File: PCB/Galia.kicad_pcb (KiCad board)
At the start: 2 copper layers, 55 x 13.5 mm, 9 parts, among them J1 USB In, J2 USB, SW1 Bootsel, SW2 Reset, U2 TPD4E05U06

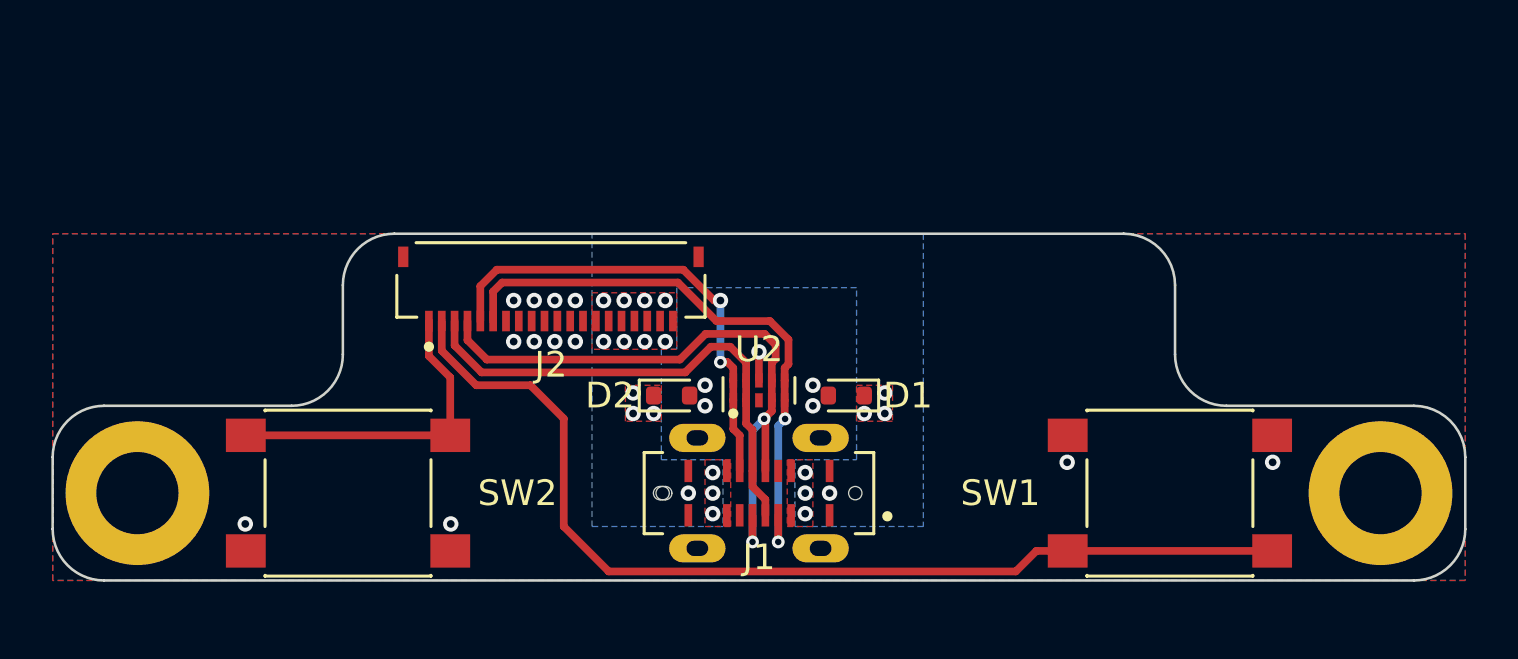
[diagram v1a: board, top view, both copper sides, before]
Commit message: 17/07/2023 update
Changed 20 pin FFC connector to 14 pin JST SH connector. Repositioned components.
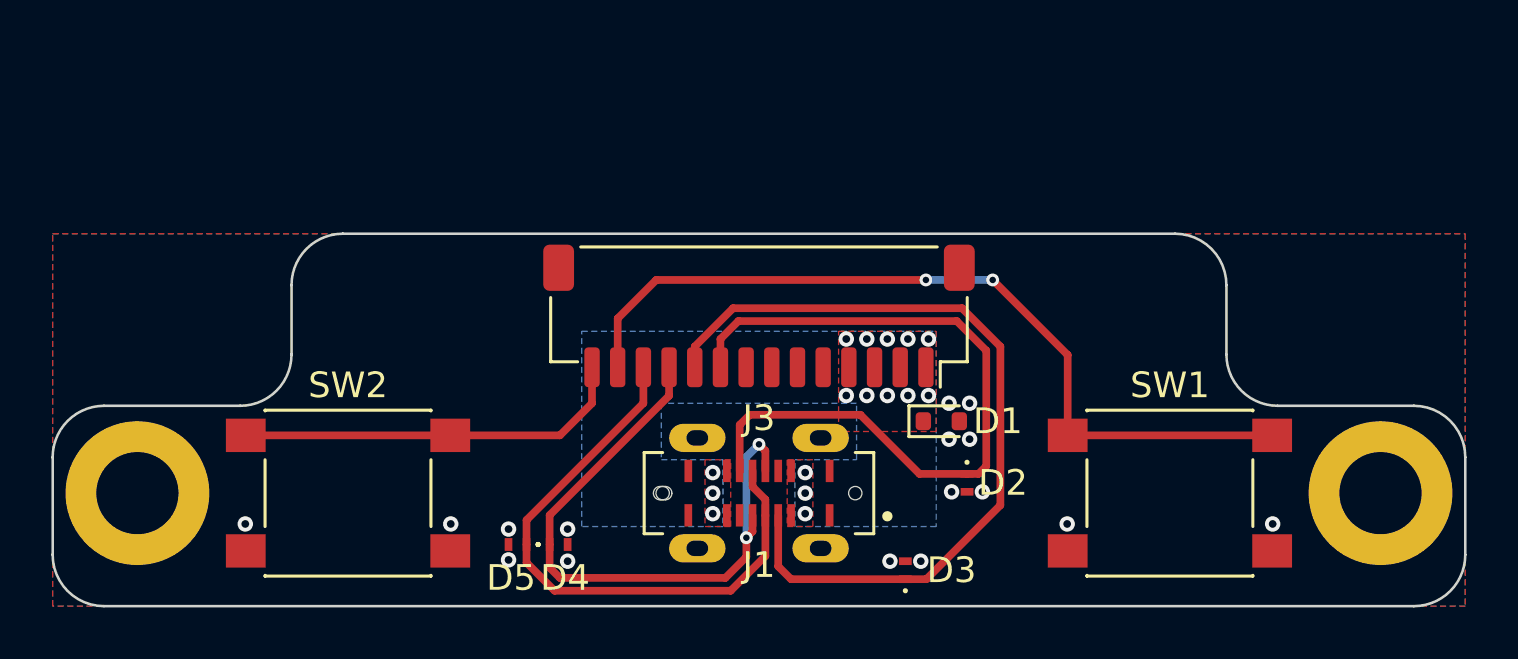
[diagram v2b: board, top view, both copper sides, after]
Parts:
- removed J2: USB, Galia:HRS_FH34SRJ-20S-0.5SH(50)
- removed U2: TPD4E05U06, Galia:USON-10_2.5x1.0mm_P0.5mm
- added D3: 5V, Galia:Texas_DPY0002A_0.6x1mm_P0.65mm, F.Cu at (95.7, 56.0)
- added D4: 5V, Galia:Texas_DPY0002A_0.6x1mm_P0.65mm, F.Cu at (82.2, 55.0)
- added D5: 5V, Galia:Texas_DPY0002A_0.6x1mm_P0.65mm, F.Cu at (80.6, 55.0)
- added J3: USB, Galia:JST_SH_SM14B-SRSS-TB_1x14-1MP_P1.00mm_Horizontal, F.Cu at (90.0, 46.1)
- D2: footprint Diode_SMD:D_SOD-523 -> Galia:Texas_DPY0002A_0.6x1mm_P0.65mm
- SW1: value Bootsel -> PTS45
- SW2: value Reset -> PTS45
- moved D2 12.0 mm to (98.1, 52.6), turned to -90 degrees
- moved D1 3.83 mm to (97.1, 50.2), turned to 0 degrees
- turned SW1 to 180 degrees
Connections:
- D2 pad 1: VBUS -> CC2
- SW1 pad 2: /BOOTSEL -> /~{RST}
- SW2 pad 2: /~{RST} -> /BOOTSEL
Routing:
- net /BOOTSEL: track 39.8 -> 15.4 mm
- net /~{RST}: track 12.8 -> 32.3 mm, vias 0 -> 2
- net CC2: track 18.6 -> 29.3 mm, vias 2 -> 0
- net CC1: track 22.8 -> 32.2 mm, vias 2 -> 0
- net /D+: track 19.7 -> 23.3 mm
- net GND: track 1.12 -> 0.00 mm, vias 19 -> 16
- net VBUS: vias 20 -> 16
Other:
- board size 55 x 13.5 mm -> 55 x 14.5 mm

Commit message: 18/07/2023 update.
Changed JST connector back to 20 pin FFC. Centered connector.
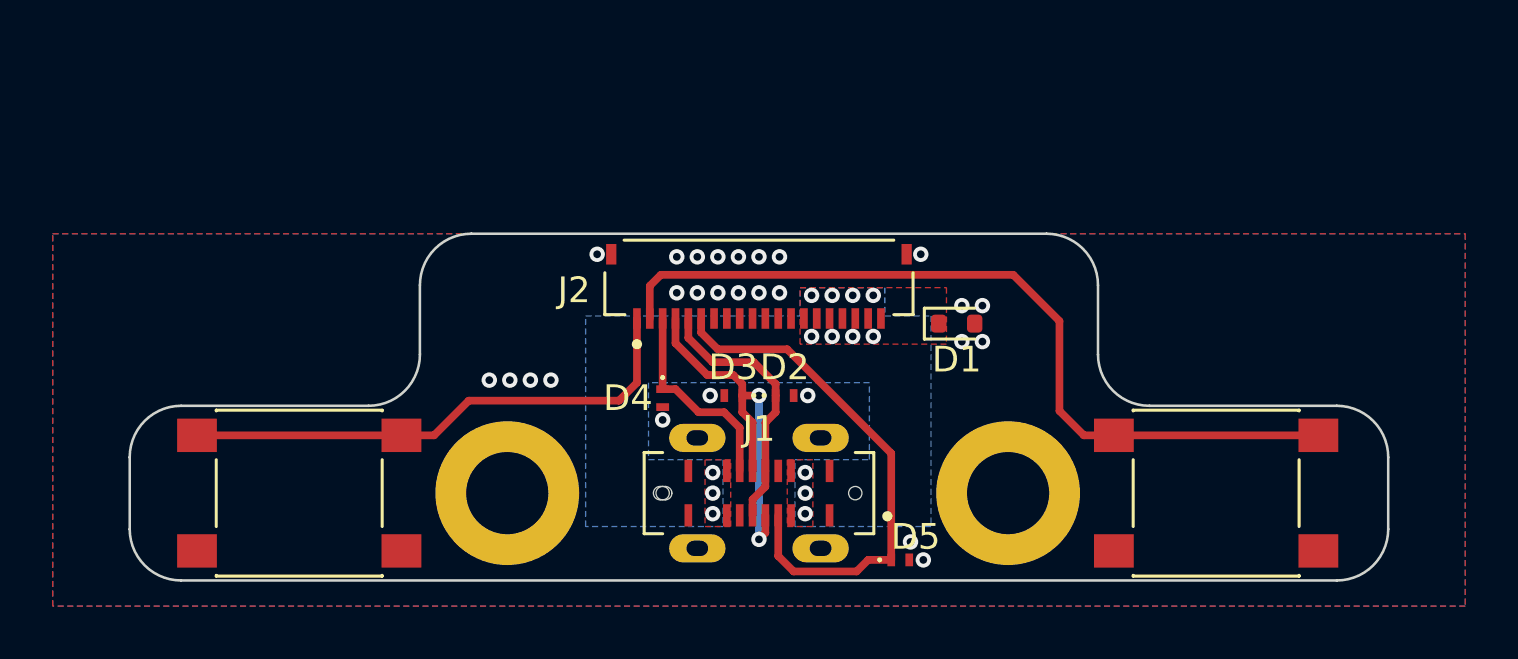
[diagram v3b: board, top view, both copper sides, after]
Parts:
- removed J3: USB, Galia:JST_SH_SM14B-SRSS-TB_1x14-1MP_P1.00mm_Horizontal
- added J2: USB, Galia:HRS_FH34SRJ-20S-0.5SH(50), F.Cu at (90.0, 43.7)
- moved D5 14.9 mm to (95.5, 55.6), turned to 0 degrees
- moved H1 14.5 mm to (99.7, 53.0)
- moved H2 14.4 mm to (80.2, 53.0)
- moved D3 9.55 mm to (89.0, 49.2), turned to 180 degrees
- moved D2 7.87 mm to (91.0, 49.2), turned to 0 degrees
- moved D4 6.99 mm to (86.2, 49.3), turned to -90 degrees
- moved D1 3.85 mm to (97.7, 46.4)
- moved SW2 1.90 mm to (72.1, 53.0)
- moved SW1 1.80 mm to (107.8, 53.0)
- renumbered H2 to H1, H1 to H2
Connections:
- D2 pad 1: CC2 -> /D-
- D3 pad 1: CC1 -> /D+
- D4 pad 1: /D- -> CC2
- D5 pad 1: /D+ -> CC1
- H1 pad 1: GND -> (no net)
- H2 pad 1: (no net) -> GND
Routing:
- net CC2: track 29.3 -> 8.05 mm
- net /D-: track 24.6 -> 10.4 mm, vias 2 -> 0
- net CC1: track 32.2 -> 20.5 mm
- net /D+: track 23.3 -> 15.0 mm, vias 0 -> 2
- net /BOOTSEL: track 15.4 -> 20.5 mm
- net /~{RST}: track 32.3 -> 32.1 mm, vias 2 -> 0
- net VBUS: vias 16 -> 14
- net GND: vias 16 -> 27
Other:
- board size 55 x 14.5 mm -> 49 x 13.5 mm

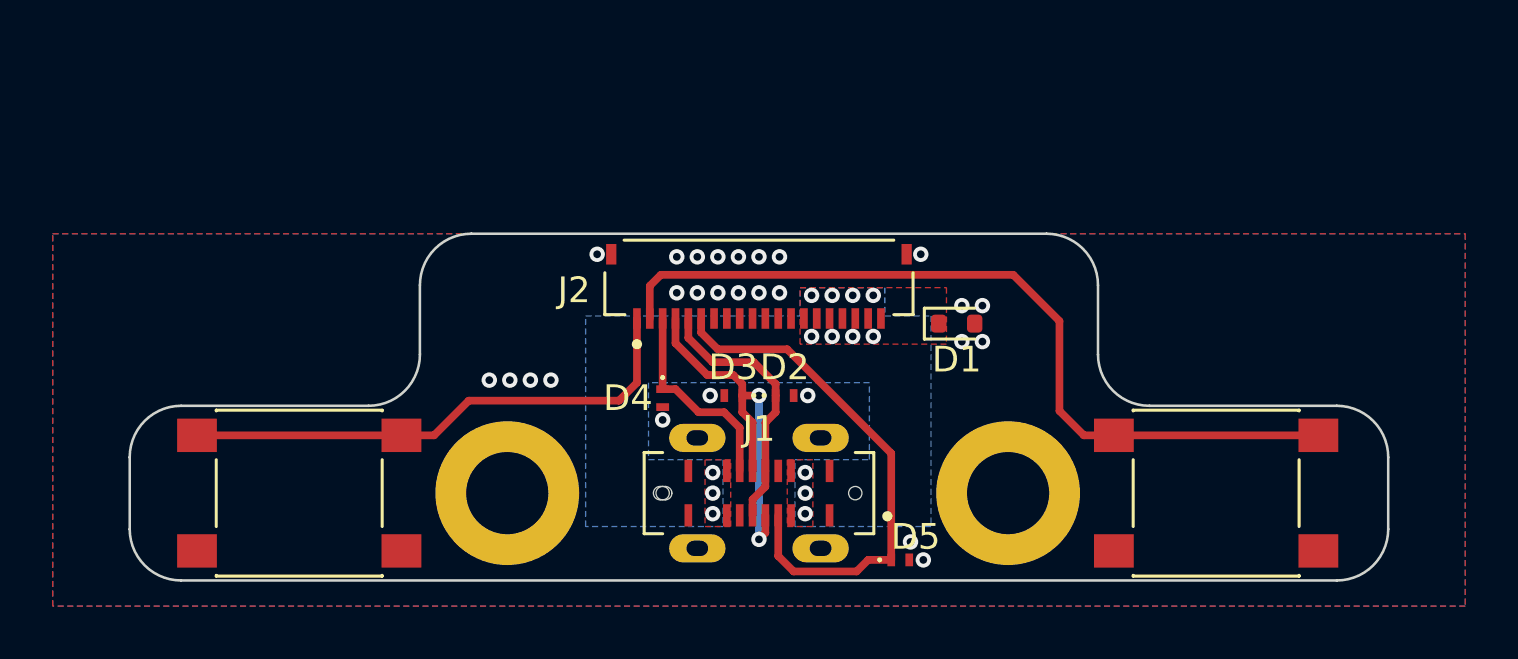
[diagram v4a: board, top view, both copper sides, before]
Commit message: 21/07/2023 update.
Changed 20 pin FFC to 7 pin and 8 pin JST SH connector. Fixed orientation.
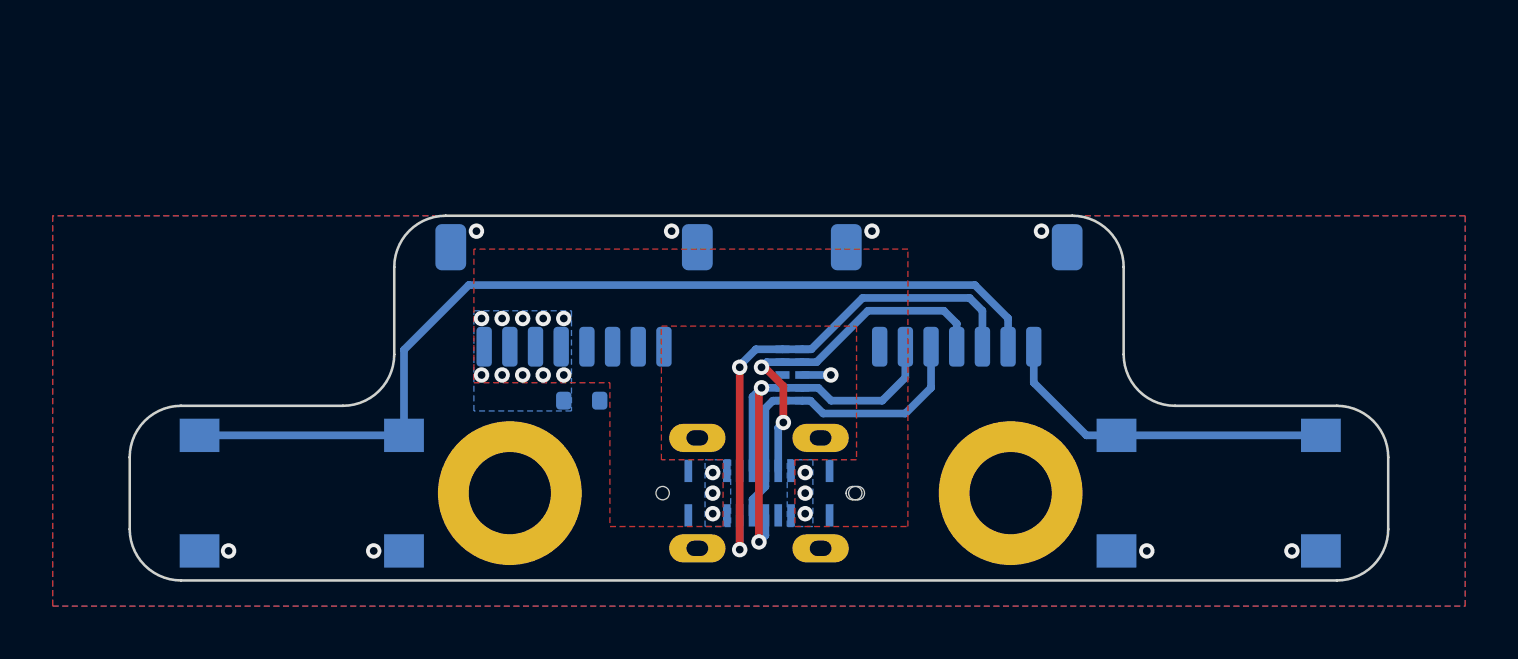
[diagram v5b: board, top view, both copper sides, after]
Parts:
- removed D2, D3, D4, D5: 5V, Galia:Texas_DPY0002A_0.6x1mm_P0.65mm
- added J3: I/O, Galia:JST_SH_SM07B-SRSS-TB_1x07-1MP_P1.00mm_Horizontal, B.Cu at (97.7, 45.3)
- added U1: TPD4E05U06, Galia:USON-10_2.5x1.0mm_P0.5mm, B.Cu at (91.3, 48.4)
- D1, J1, SW1, SW2: moved to B.Cu
- H1: renamed from H2; moved to B.Cu
- H2: renamed from H1; moved to B.Cu
- J2: value USB -> Power; footprint Galia:HRS_FH34SRJ-20S-0.5SH(50) -> Galia:JST_SH_SM08B-SRSS-TB_1x08-1MP_P1.00mm_Horizontal; moved to B.Cu
- moved SW2 35.8 mm to (107.9, 53.0), turned to 0 degrees
- moved SW1 35.6 mm to (72.2, 53.0), turned to 0 degrees
- moved H1 19.6 mm to (99.8, 53.0), turned to 180 degrees
- moved H2 19.4 mm to (80.3, 53.0), turned to 180 degrees
- moved D1 14.9 mm to (83.1, 49.4)
- moved J2 7.38 mm to (82.8, 45.3), turned to 0 degrees
- turned J1 to 0 degrees
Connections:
- H1 pad 1: GND -> (no net)
- H2 pad 1: (no net) -> GND
- J2 pad 1: /BOOTSEL -> VBUS
- J2 pad 2: /~{RST} -> VBUS
- J2 pad 3: CC2 -> VBUS
- J2 pad 4: /D+ -> VBUS
- J2 pad 5: /D- -> GND
- J2 pad 6: CC1 -> GND
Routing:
- net /D-: track 10.4 -> 18.1 mm, vias 0 -> 2
- net /BOOTSEL: track 20.5 -> 13.4 mm
- net CC2: track 8.05 -> 14.2 mm, vias 0 -> 2
- net /~{RST}: track 32.1 -> 37.5 mm
- net /D+: track 15.0 -> 13.2 mm, vias 2 -> 0
- net GND: track 0.00 -> 1.11 mm, vias 27 -> 9
- net CC1: track 20.5 -> 20.7 mm, vias 0 -> 2
- net VBUS: vias 14 -> 16
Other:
- board size 49 x 13.5 mm -> 49 x 14.2 mm

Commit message: 25/07/2023 update
Changed 8 pin JST SH connector to 6 pin. Changed orientation of SH connectors for easier routing of wires. Added Ariamelon logo. Added PCB cutouts to allow for buttons to be snapped off.
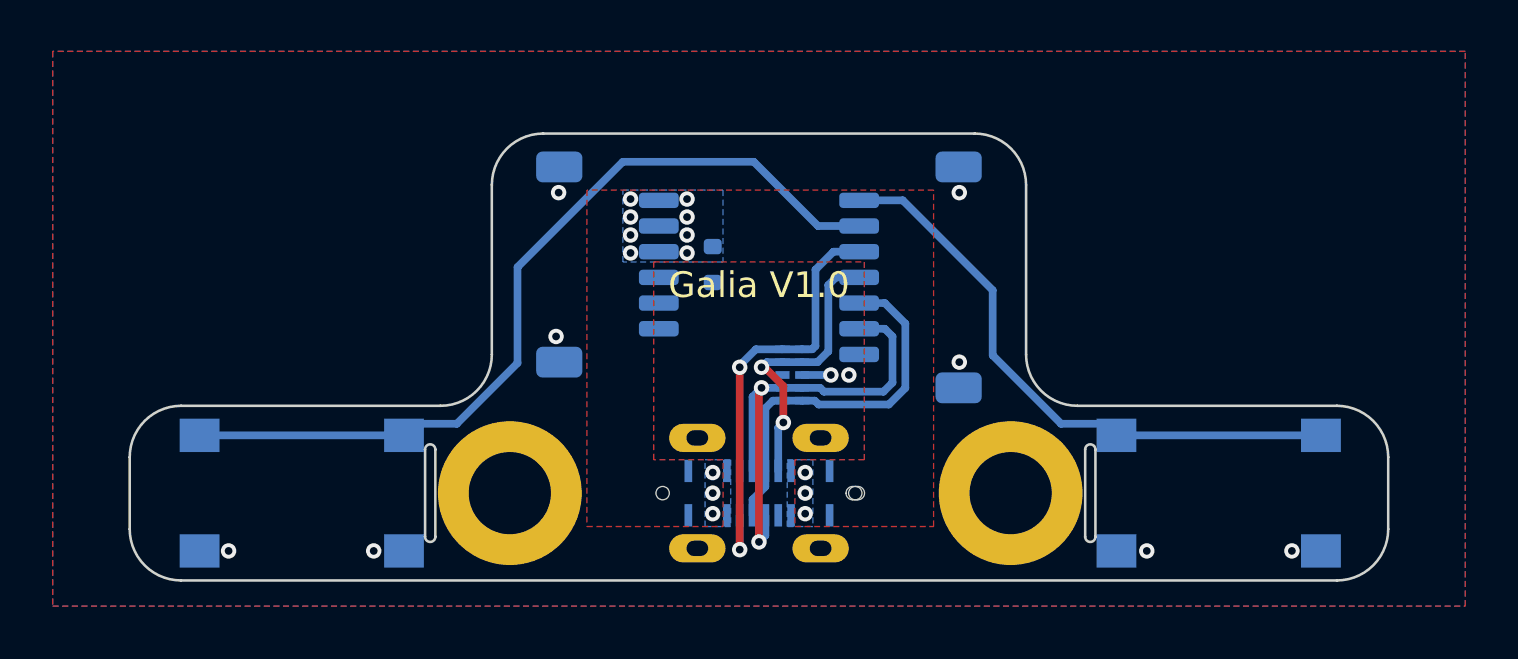
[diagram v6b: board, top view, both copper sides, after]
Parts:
- added A1: Ariamelon Logo, Galia:Ariamelon_Logo_Mask, F.Cu at (90.0, 42.6)
- J2: footprint Galia:JST_SH_SM08B-SRSS-TB_1x08-1MP_P1.00mm_Horizontal -> Galia:JST_SH_SM06B-SRSS-TB_1x06-1MP_P1.00mm_Horizontal
- moved D1 7.36 mm to (88.2, 44.1), turned to -90 degrees
- moved J3 1.93 mm to (95.9, 44.6), turned to -90 degrees
- moved J2 1.77 mm to (84.1, 44.1), turned to 90 degrees
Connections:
- J2 pad 1: VBUS -> GND
- J2 pad 2: VBUS -> GND
- J2 pad 3: VBUS -> GND
- J2 pad 5: GND -> VBUS
- J2 pad 6: GND -> VBUS
- J3 pad 1: GND -> /BOOTSEL
- J3 pad 2: /D- -> /~{RST}
- J3 pad 3: /D+ -> CC1
- J3 pad 5: CC1 -> /D+
- J3 pad 6: /~{RST} -> /D-
- J3 pad 7: /BOOTSEL -> GND
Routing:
- net /BOOTSEL: track 13.4 -> 22.6 mm
- net /~{RST}: track 37.5 -> 33.2 mm
- net CC1: track 20.7 -> 17.2 mm
- net CC2: track 14.2 -> 11.8 mm
- net /D+: track 13.2 -> 14.9 mm
- net /D-: track 18.1 -> 19.2 mm
- net VBUS: vias 16 -> 14
- net GND: vias 9 -> 10
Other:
- board size 49 x 14.2 mm -> 49 x 17.4 mm
- board text added: "Galia V1.0"

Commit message: 26/07/2023 update
Fixed position of button and mounting holes. Added JLC tooling holes.
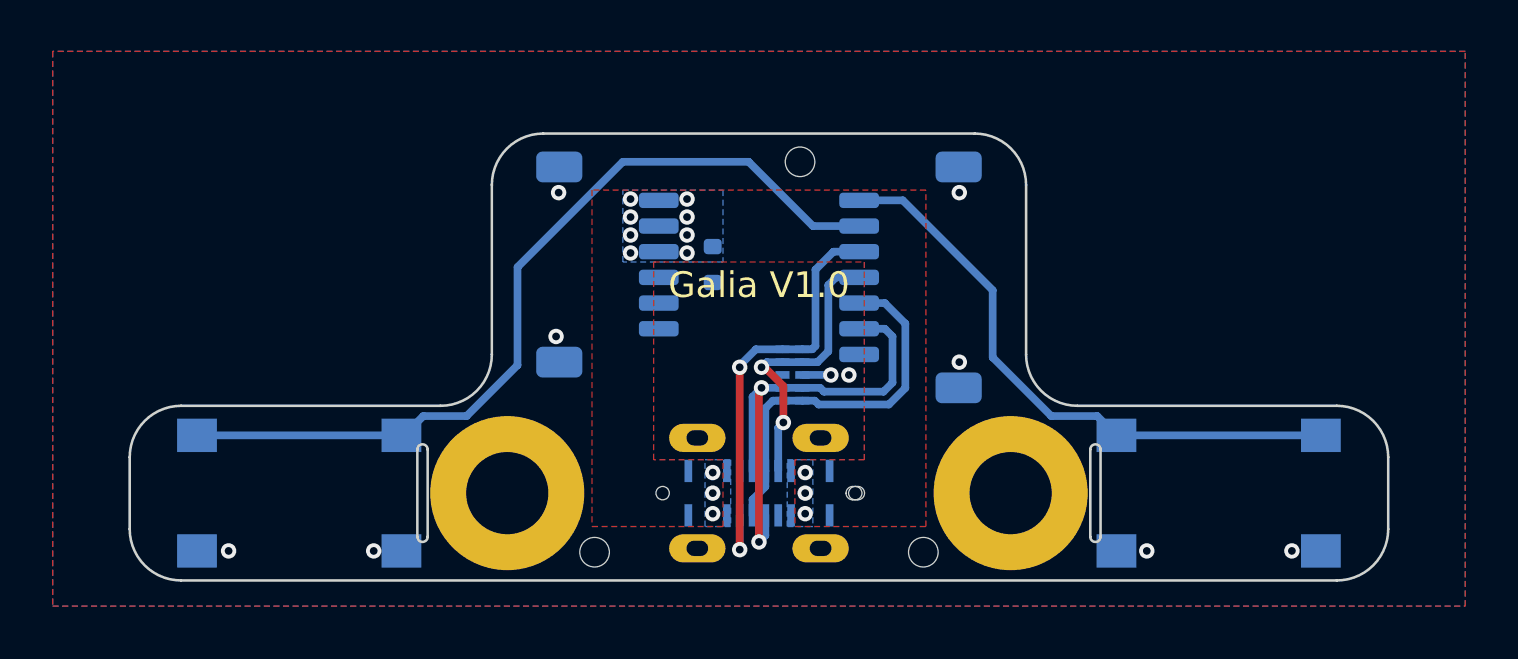
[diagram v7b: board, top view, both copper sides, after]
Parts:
- added H3: Tooling Hole, Galia:JLC Tooling Hole, F.Cu at (83.6, 55.3)
- added H4: Tooling Hole, Galia:JLC Tooling Hole, F.Cu at (91.6, 40.1)
- added H5: Tooling Hole, Galia:JLC Tooling Hole, F.Cu at (96.4, 55.3)
- SW1, SW2: value PTS45 -> PTS645
- moved SW1 0.10 mm to (72.1, 53.0)
- moved H2 0.10 mm to (80.2, 53.0)
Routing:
- net /BOOTSEL: track 22.6 -> 23.3 mm
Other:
- outline, holes or cut-outs redrawn
